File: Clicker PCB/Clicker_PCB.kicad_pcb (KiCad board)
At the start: 4 copper layers, 30 x 85.5 mm, 122 parts, among them J1 Pogo, J2 IPX, SW1 CLICKER, SW3 BTN, SW4 BTN, U1 STM32WB07CCV6, U2 MLPF-NRG-01D3, U3 MCP73833, U4 ISL91127IR, U5 DW1000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

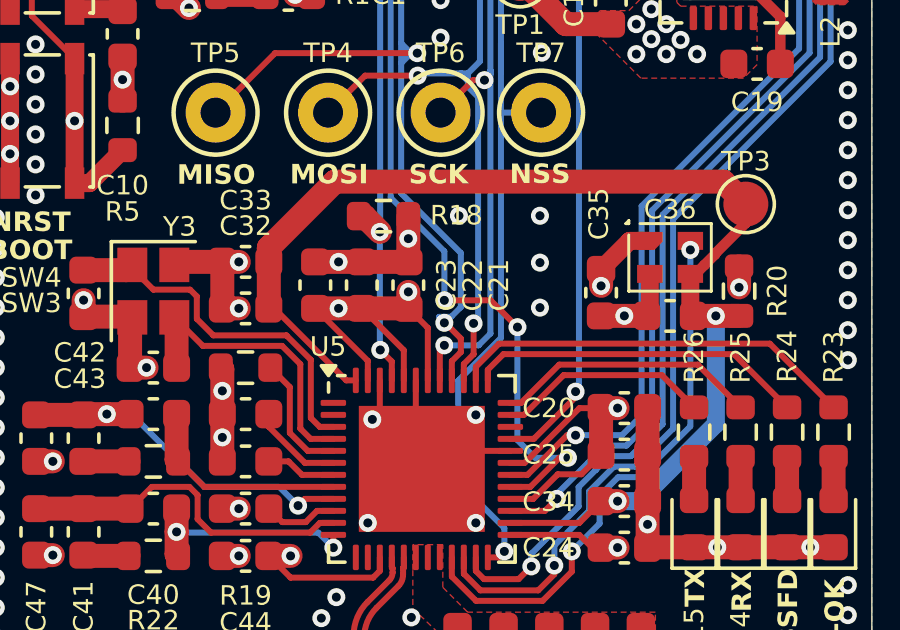
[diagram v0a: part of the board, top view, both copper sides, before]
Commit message: Updated PCB, Beacon-Visualizer, Code Explaination, User Manual, and added back- & frontend.
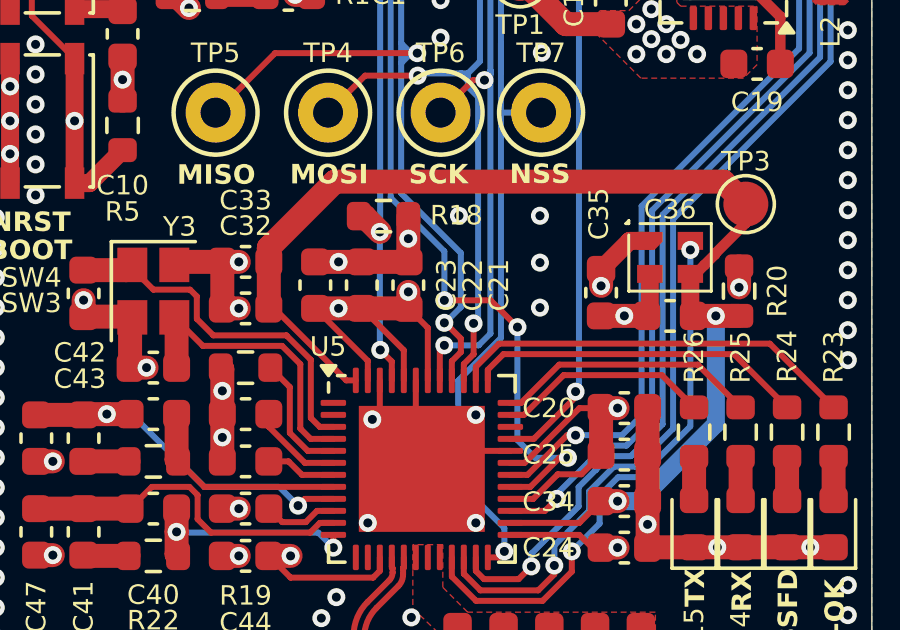
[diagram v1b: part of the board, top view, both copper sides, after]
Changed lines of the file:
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@@
 		(grid_origin 105.3 92.275)
 		(pcbplotparams
-			(layerselection 0x00010fc_ffffffff)
+			(layerselection 0x00010ff_ffffffff)
 			(plot_on_all_layers_selection 0x0000000_00000000)
 			(disableapertmacros no)
@@
 			(outputformat 1)
 			(mirror no)
-			(drillshape 1)
+			(drillshape 0)
 			(scaleselection 1)
-			(outputdirectory "")
+			(outputdirectory "gerber/")
 		)
 	)
@@
 	)
 	(segment
-		(start 121.6 145.077208)
-		(end 119.6125 143.089708)
+		(start 121.05 147.406583)
+		(end 121.077815 147.406583)
 		(width 0.2)
 		(layer "B.Cu")
@@
 	)
 	(segment
-		(start 121.6 146.884398)
-		(end 121.6 145.077208)
+		(start 119.6125 138.0875)
+		(end 119.6125 129.160417)
 		(width 0.2)
 		(layer "B.Cu")
@@
 	)
 	(segment
-		(start 119.6125 138.0875)
-		(end 119.6125 129.160417)
+		(start 119.6125 143.089708)
+		(end 119.6125 138.75)
 		(width 0.2)
 		(layer "B.Cu")
@@
 	)
 	(segment
-		(start 121.05 147.406583)
-		(end 121.077815 147.406583)
+		(start 121.6 146.884398)
+		(end 121.6 145.077208)
 		(width 0.2)
 		(layer "B.Cu")
@@
 	)
 	(segment
-		(start 120.877812 147.20658)
-		(end 121.277818 147.20658)
-		(width 0.2)
-		(layer "B.Cu")
-		(net 84)
-	)
-	(segment
 		(start 119.6125 138.375)
 		(end 119.6125 138.0875)
@@
 	)
 	(segment
-		(start 125 123.772917)
-		(end 125 113.15704)
+		(start 121.6 145.077208)
+		(end 119.6125 143.089708)
 		(width 0.2)
 		(layer "B.Cu")
@@
 	)
 	(segment
-		(start 121.277818 147.20658)
+		(start 121.077815 147.406583)
 		(end 121.6 146.884398)
 		(width 0.2)
@@
 	)
 	(segment
-		(start 121.077815 147.406583)
-		(end 120.877812 147.20658)
+		(start 125 123.772917)
+		(end 125 113.15704)
 		(width 0.2)
 		(layer "B.Cu")
@@
 		(width 0.2)
 		(layer "B.Cu")
-		(net 84)
-	)
-	(segment
-		(start 119.6125 143.089708)
-		(end 119.6125 138.75)
-		(width 0.2)
-		(layer "B.Cu")
